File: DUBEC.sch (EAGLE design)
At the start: 68 parts

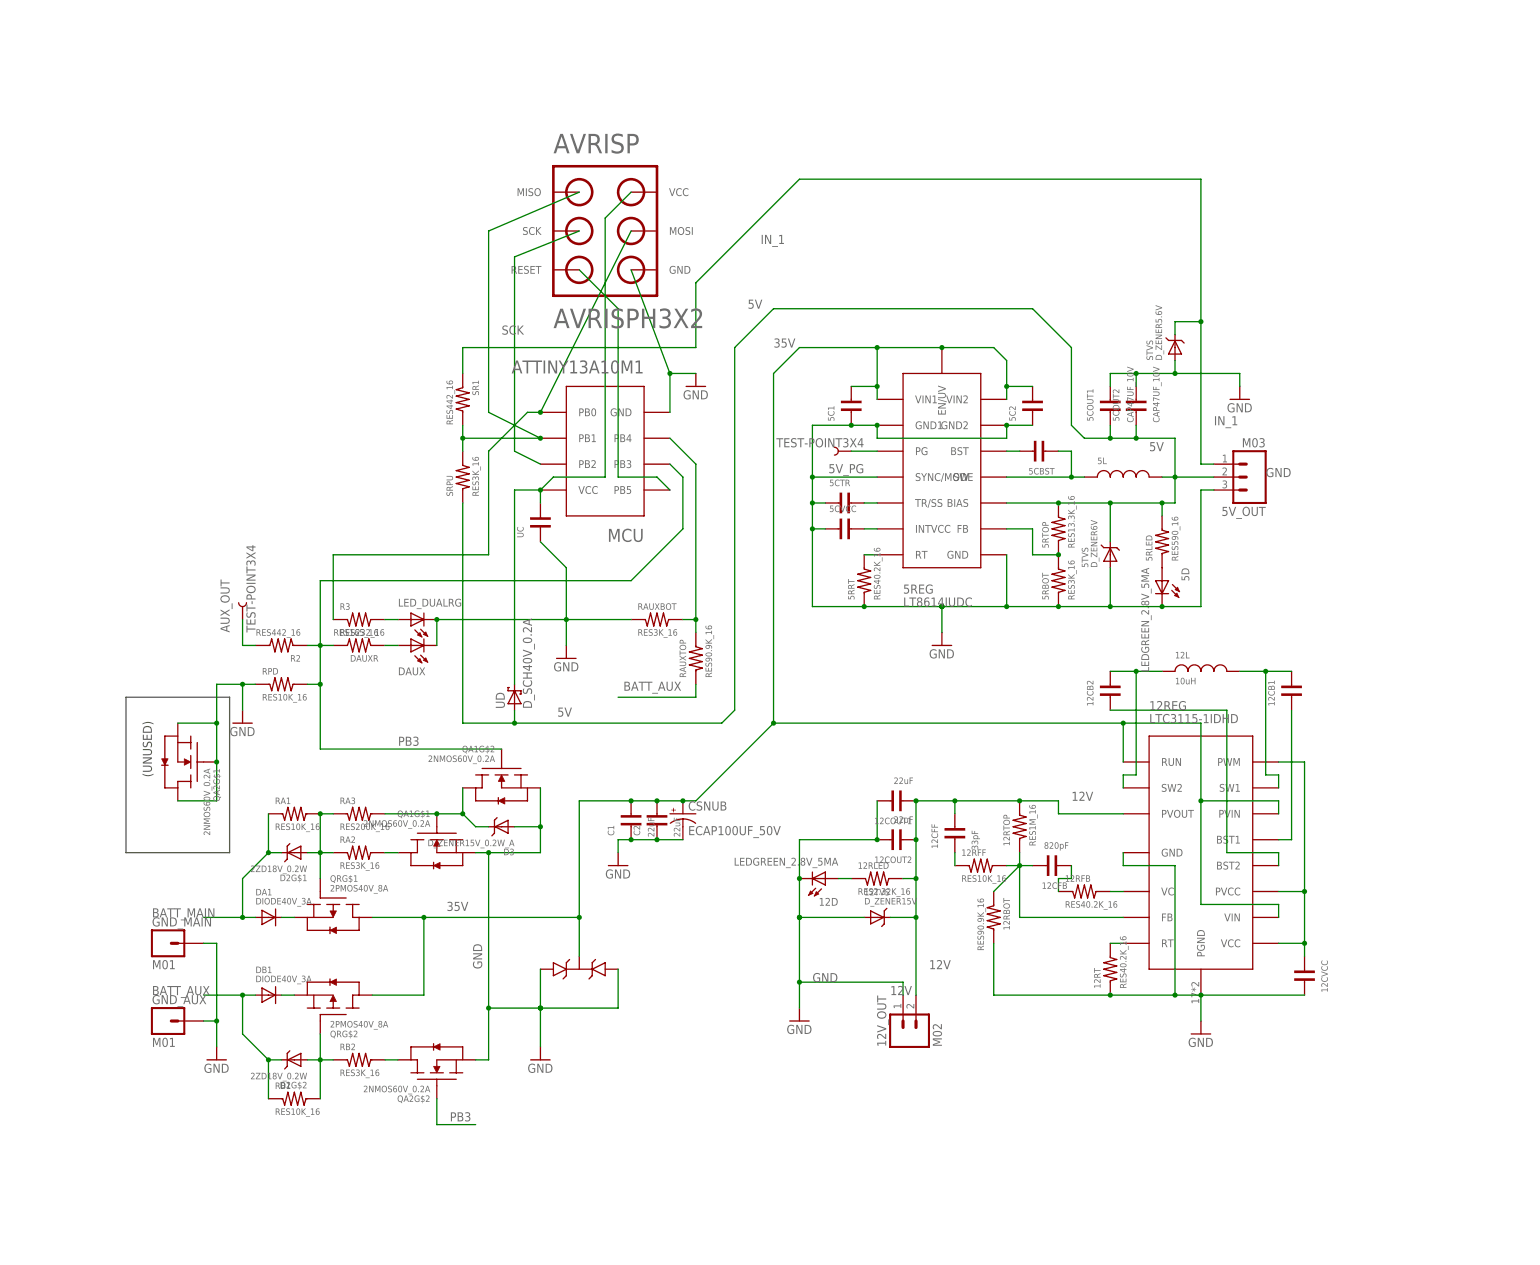
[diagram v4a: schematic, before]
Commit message: Tidying schematic
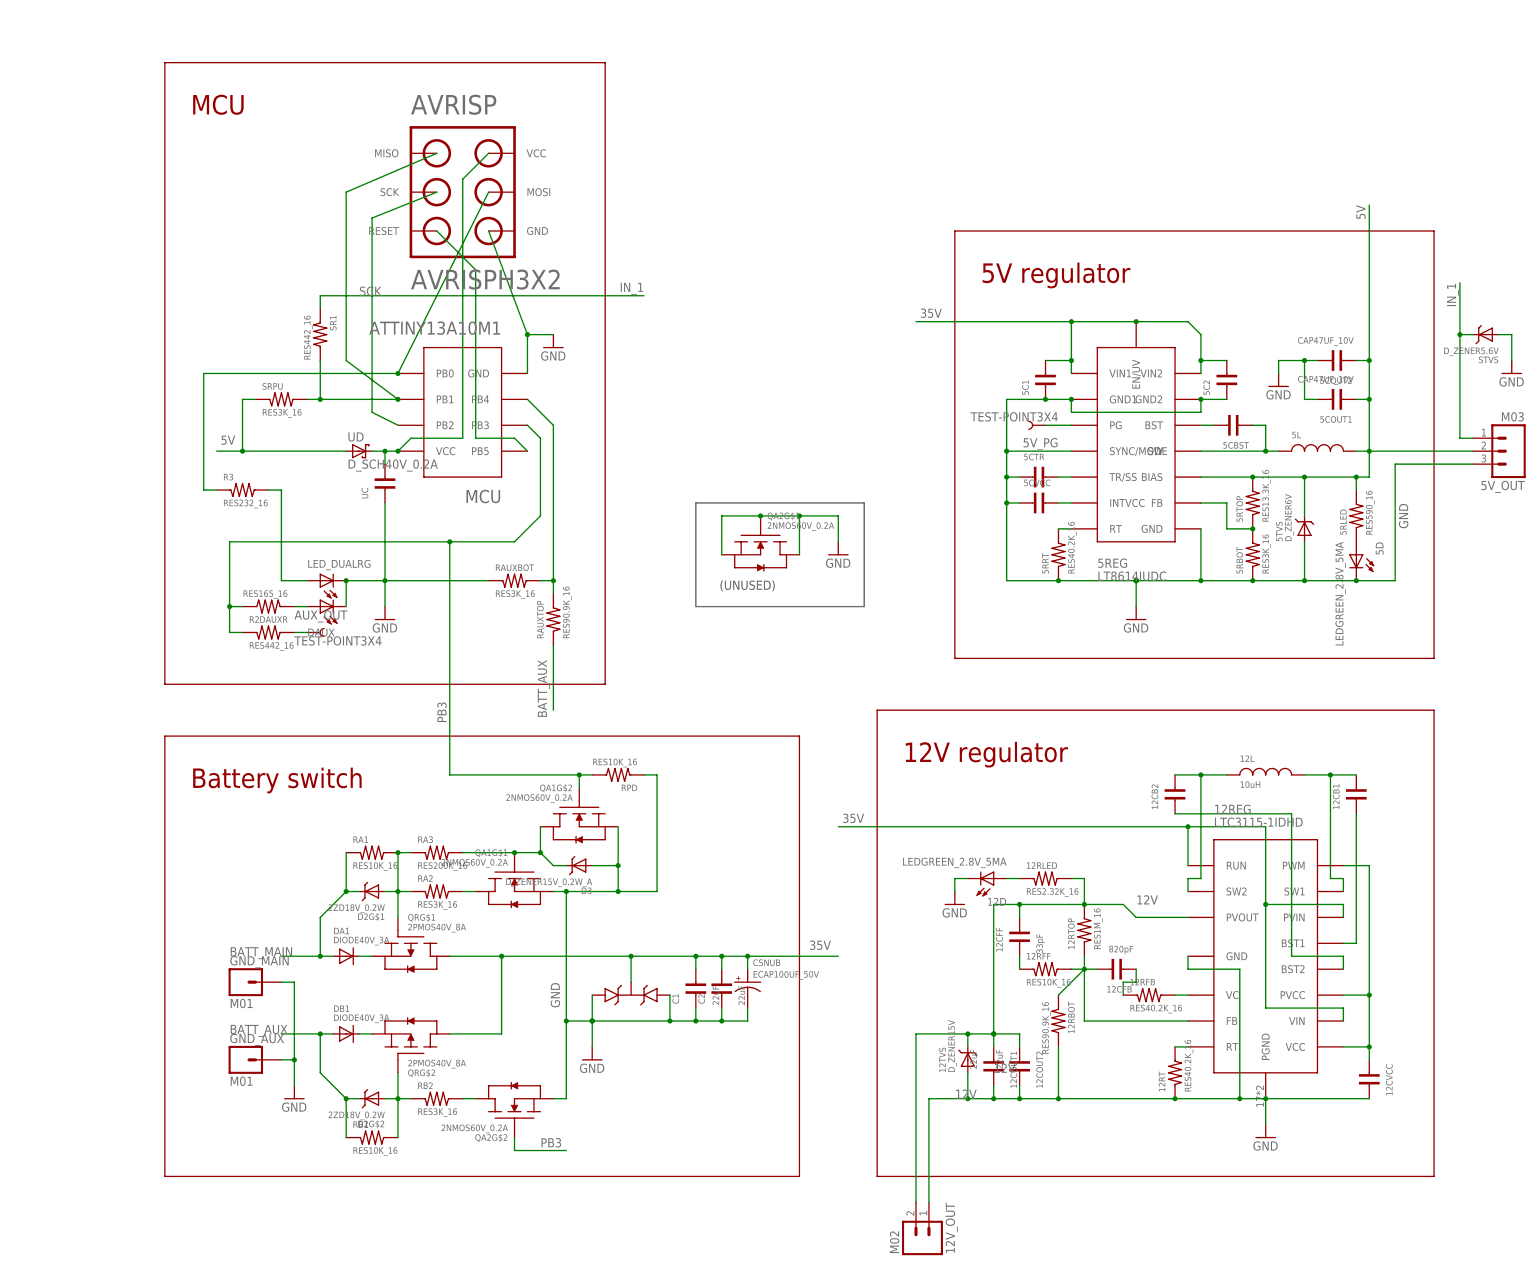
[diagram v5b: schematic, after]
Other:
- note added: "12V regulator"
- note added: "5V regulator"
- note added: "Battery switch"
- note added: "MCU"
- moved on the sheet: 12CB1, 12CB2, 12CFB, 12CFF, 12COUT1, 12COUT2, 12CVCC, 12D, 12L, 12RBOT, 12REG, 12RFB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

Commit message: 12V RUN toggle
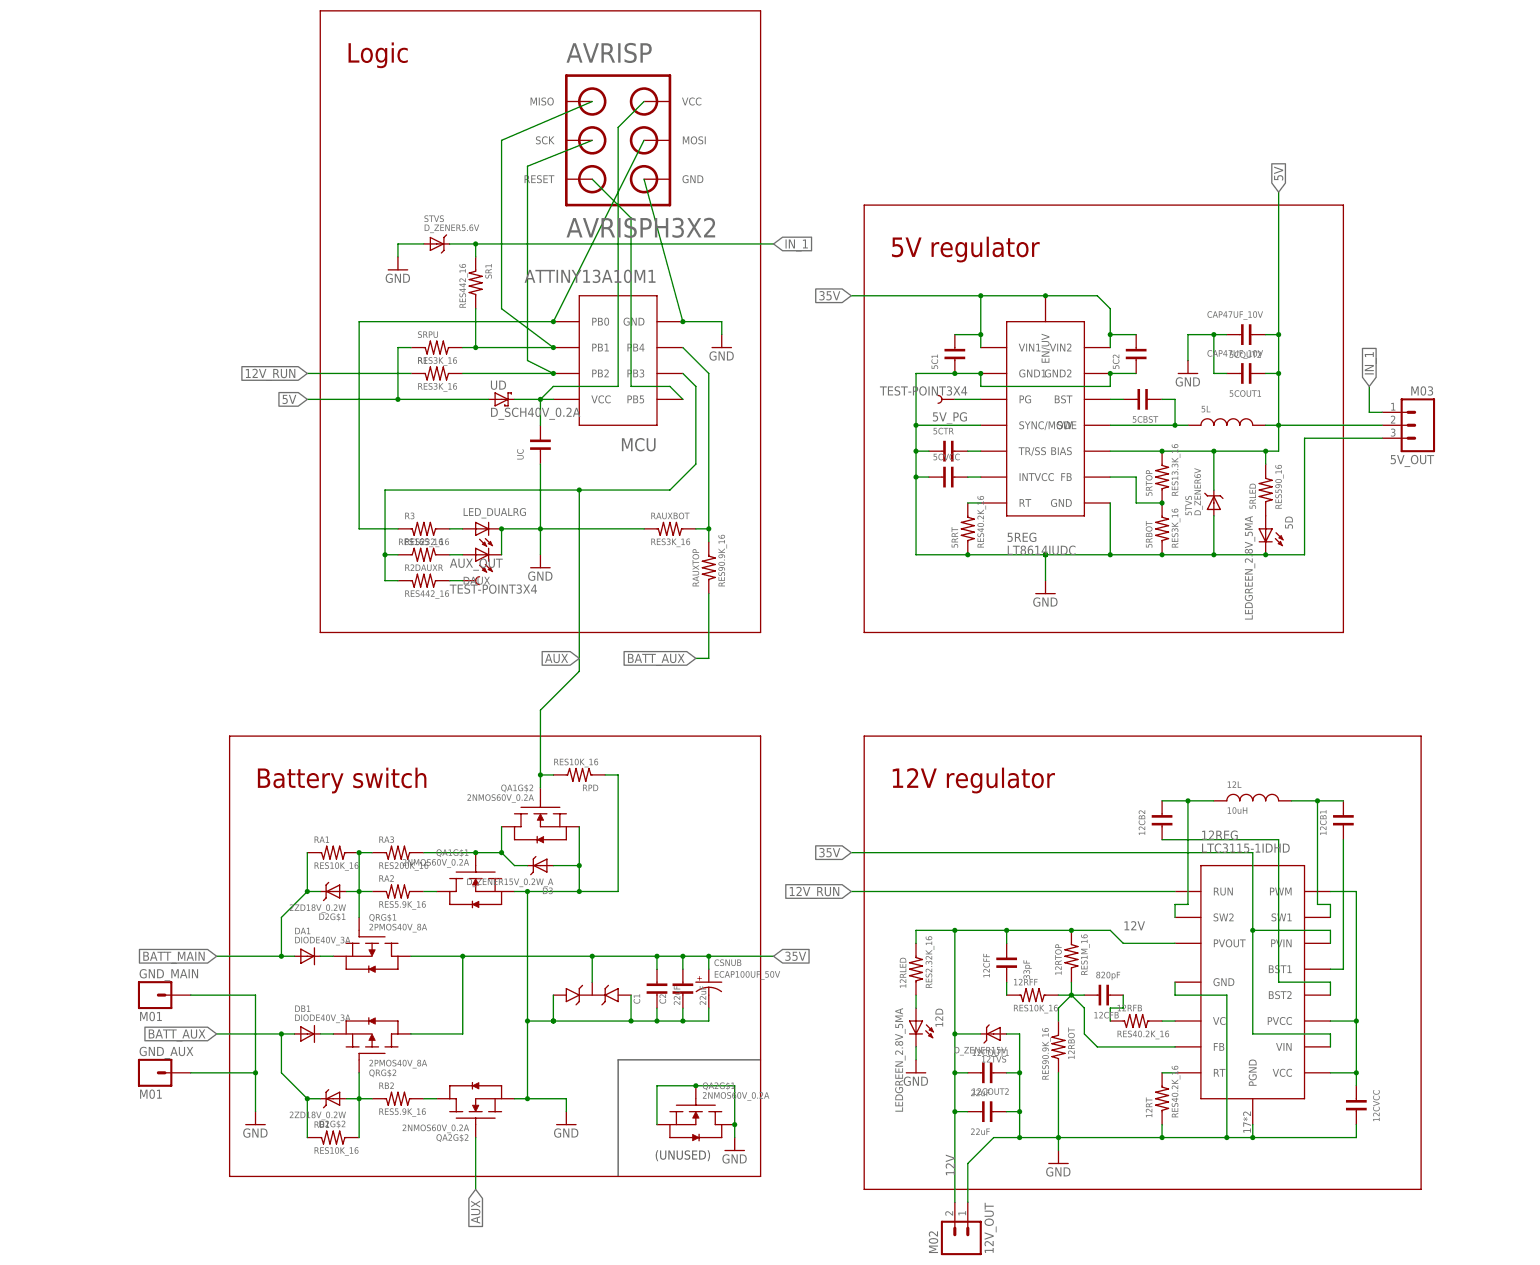
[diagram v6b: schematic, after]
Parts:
- added R1: RES3K_16, dubec:RES3K_16
- RA2, RB2: value RES3K_16 -> RES5.9K_16; device dubec:RES3K_16 -> dubec:RES5.9K_16
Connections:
- net PB3 renamed AUX
- new net 12V_RUN: 12REG.RUN, R1.1
- net 35V: no longer 12REG.RUN
- net SCK: now also R1.2
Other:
- note added: "Logic"
- note removed: "MCU"
- moved on the sheet: 12CB1, 12CB2, 12CFB, 12CFF, 12COUT1, 12COUT2, 12CVCC, 12D, 12L, 12RBOT, 12REG, 12RFB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

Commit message: Tidying
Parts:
- SR1: value RES442_16 -> RES232_16; device dubec:RES442_16 -> dubec:RES232_16
- SRPU: value RES3K_16 -> RES10K_16; device dubec:RES3K_16 -> dubec:RES10K_16
- renumbered UC to CMCU
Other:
- moved on the sheet: R1, SR1, SRPU, STVS

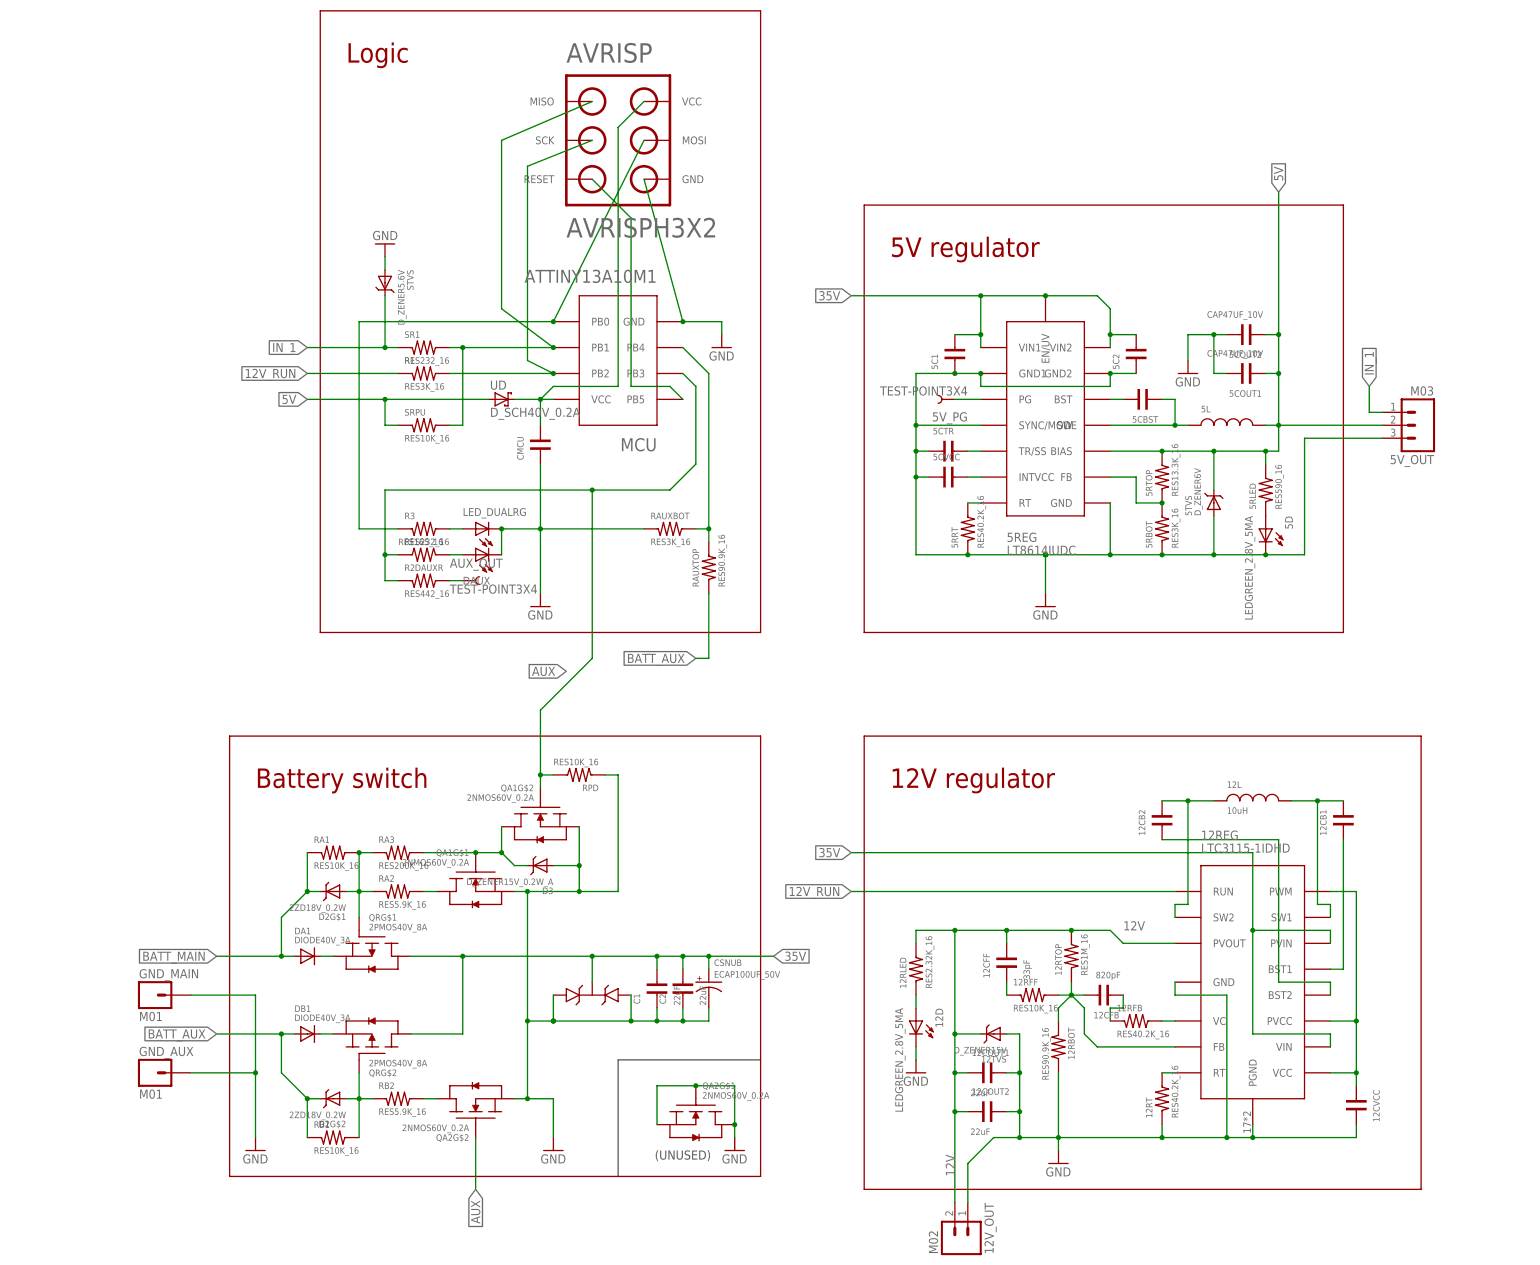
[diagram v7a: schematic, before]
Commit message: 12V run pull-up
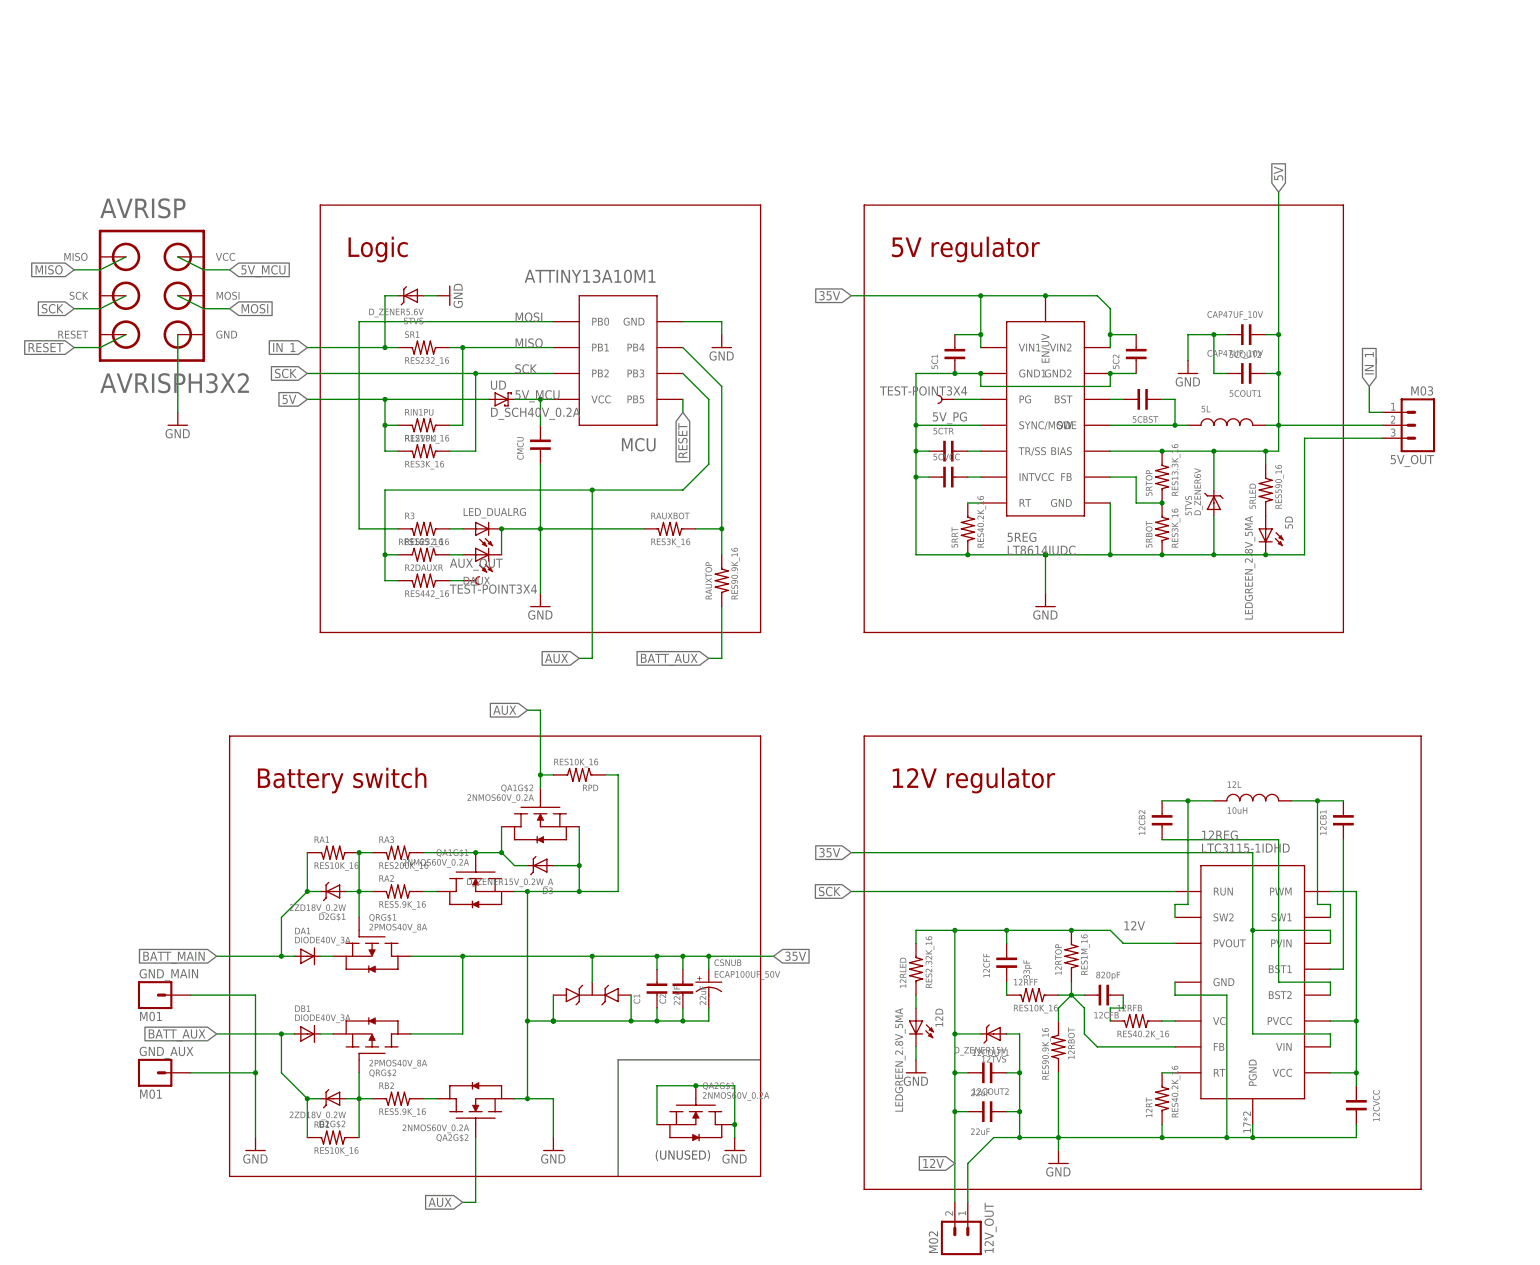
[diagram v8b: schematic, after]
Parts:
- removed R1: RES3K_16, dubec:RES3K_16
- added R12VPU: RES3K_16, dubec:RES3K_16
- renumbered SRPU to RIN1PU
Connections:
- removed net 12V_RUN: 12REG.RUN, R1.1
- net 5V: now also R12VPU.1
- net SCK: now also 12REG.RUN, R12VPU.2; no longer R1.2
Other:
- moved on the sheet: AVRISP, RAUXTOP, STVS
